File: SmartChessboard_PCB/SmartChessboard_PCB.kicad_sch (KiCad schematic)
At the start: 24 parts, among them J1 USB_C_Receptacle, SW1 SMD_4.6x2.8mm_h2.5mm, SW2 SMD_4.6x2.8mm_h2.5mm, U2 DT1042-04SO, U3 ESP32-S3-MINI, U6 RT9080-3.3

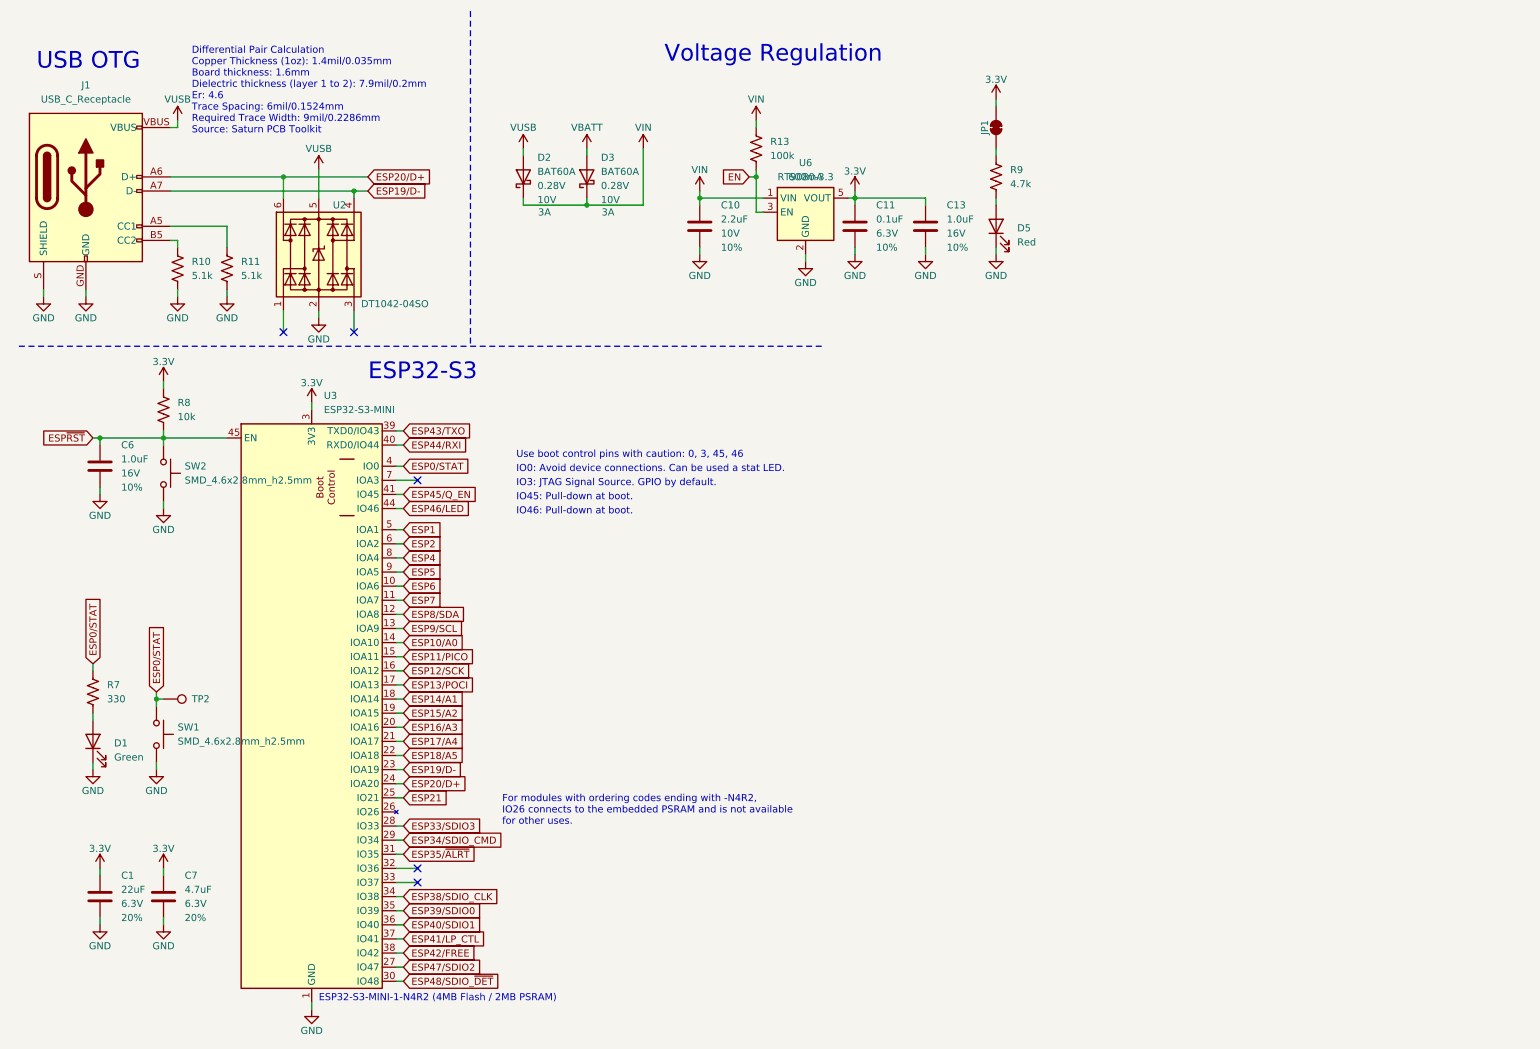
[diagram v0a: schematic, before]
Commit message: LEDs added
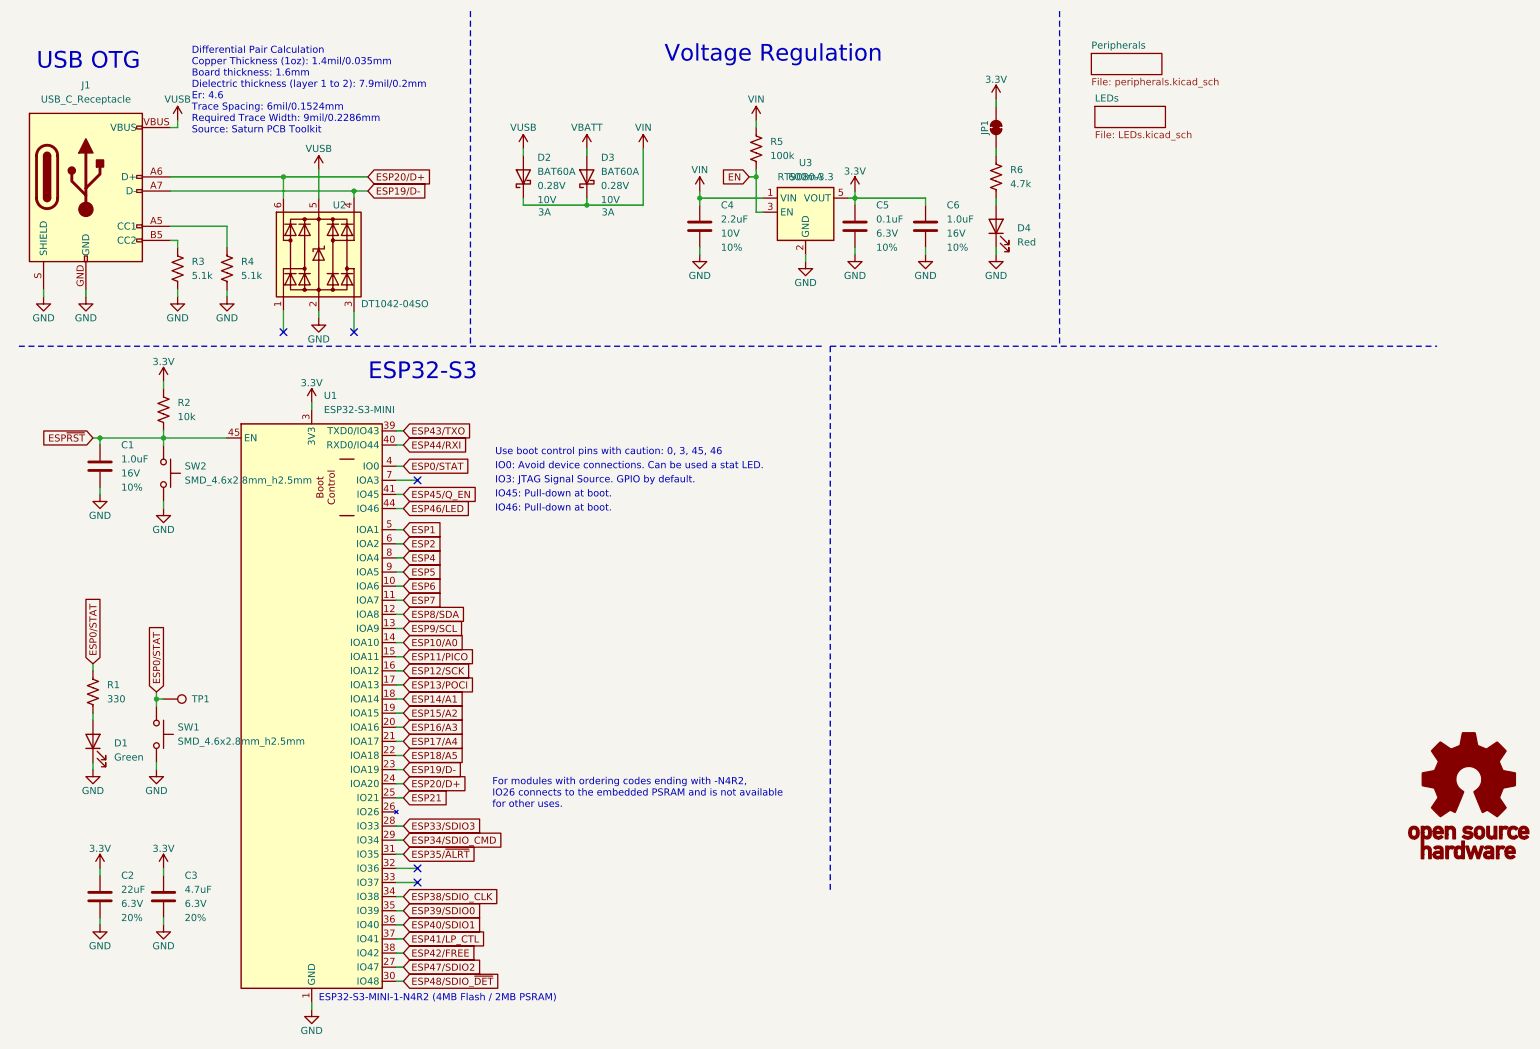
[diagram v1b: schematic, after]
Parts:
- added G1: OSHW_Logo, SparkFun-Aesthetic:Creative_Commons_License, symbol SparkFun-Aesthetic:OSHW_Logo
- renumbered C6 to C1, C1 to C2, C7 to C3, C10 to C4, C11 to C5, C13 to C6, D5 to D4, R7 to R1, R8 to R2, R10 to R3, R11 to R4, R13 to R5, R9 to R6, TP2 to TP1, U3 to U1, U6 to U3
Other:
- added sheet LEDs (LEDs.kicad_sch)
- added sheet Peripherals (peripherals.kicad_sch)

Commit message: before hall sensors
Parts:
- added J4, J5: Conn_01x15, SparkFun-Connector:1x15, symbol SparkFun-Connector:Conn_01x15
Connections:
- net 3.3V: now also J4.14 (Pin_14)
- net EN: now also J5.11 (Pin_11)
- net ESP1: now also J5.3 (Pin_3)
- net ESP10/A0: now also J4.12 (Pin_12)
- net ESP11/PICO: now also J4.5 (Pin_5)
- net ESP12/SCK: now also J4.6 (Pin_6)
- net ESP13/POCI: now also J4.4 (Pin_4)
- net ESP14/A1: now also J4.11 (Pin_11)
- net ESP15/A2: now also J4.10 (Pin_10)
- net ESP16/A3: now also J4.9 (Pin_9)
- net ESP17/A4: now also J4.8 (Pin_8)
- net ESP18/A5: now also J4.7 (Pin_7)
- net ESP2: now also J5.4 (Pin_4)
- net ESP21: now also J5.9 (Pin_9)
- net ESP4: now also J5.5 (Pin_5)
- net ESP42/FREE: now also J4.1 (Pin_1)
- net ESP43/TXO: now also J4.2 (Pin_2)
- net ESP44/RXI: now also J4.3 (Pin_3)
- net ESP5: now also J5.6 (Pin_6)
- net ESP6: now also J5.7 (Pin_7)
- net ESP7: now also J5.8 (Pin_8)
- net ESP8/SDA: now also J5.2 (Pin_2)
- net ESP9/SCL: now also J5.1 (Pin_1)
- net ESP~{RST}: now also J4.15 (Pin_15)
- net GND: now also J4.13 (Pin_13)
- net VBATT: now also J5.12 (Pin_12)
- net VUSB: now also J5.10 (Pin_10)
- net VIN renamed 5V
- no-connect marks 5 -> 8
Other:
- added sheet Hall sensors (hall.kicad_sch)
- note removed: "For modules with ordering codes ending with -N4R2, IO26 connects to the embedded PSRAM and is not available for other uses."
- moved on the sheet: D2, D3

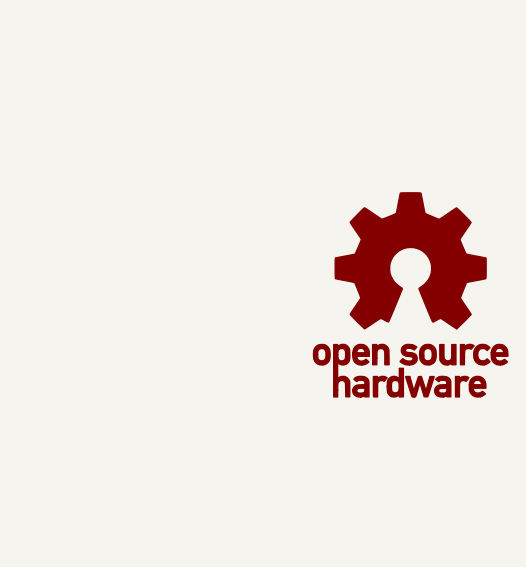
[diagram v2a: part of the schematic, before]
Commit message: level shifter added
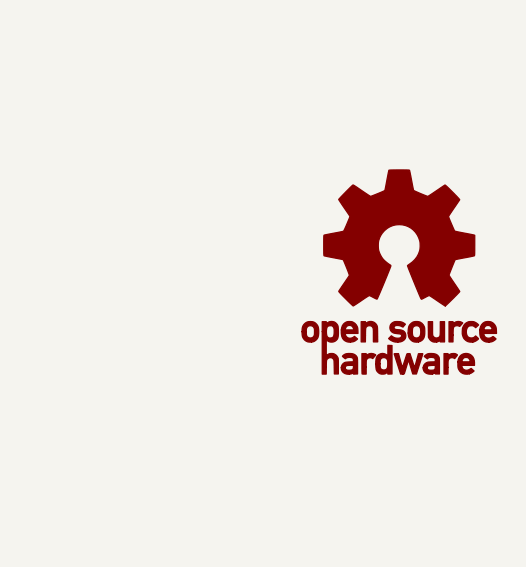
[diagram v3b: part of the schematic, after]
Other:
- title: (none) -> SmartChessboard
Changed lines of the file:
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@@
 	(generator_version "9.0")
 	(paper "A4")
+	(title_block
+		(title "SmartChessboard")
+		(date "2025-08-15")
+		(rev "0")
+		(comment 3 "Released under CERN Open Hardware Licence Version 2")
+		(comment 4 "Designed by: Alessandro Sabbadini")
+	)
 	(text "IO0: Avoid device connections. Can be used a stat LED."
 		(exclude_from_sim no)
@@
 	(symbol
 		(lib_id "SparkFun-Aesthetic:OSHW_Logo")
-		(at 273.05 157.48 0)
+		(at 271.78 154.94 0)
 		(unit 1)
 		(exclude_from_sim no)
@@
 		(fields_autoplaced yes)
 		(property "Reference" "G1"
-			(at 273.05 140.97 0)
+			(at 271.78 138.43 0)
 			(effects
 				(font
@@
 		)
 		(property "Value" "OSHW_Logo"
-			(at 273.05 166.37 0)
+			(at 271.78 163.83 0)
 			(effects
 				(font
@@
 		)
 		(property "Footprint" "SparkFun-Aesthetic:Creative_Commons_License"
-			(at 273.2547 157.5043 0)
+			(at 271.9847 154.9643 0)
 			(effects
 				(font
@@
 		)
 		(property "Datasheet" ""
-			(at 273.2547 157.5043 0)
+			(at 271.9847 154.9643 0)
 			(effects
 				(font
@@
 		)
 		(property "Description" ""
-			(at 273.05 157.48 0)
-			(effects
-				(font
+			(at 271.78 154.94 0)
+			(effects
+				(font

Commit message: psc
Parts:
- removed D2, D3: BAT60A, SparkFun-Semiconductor-Standard:SOD-323, symbol SparkFun-DiscreteSemi:D_Schottky_3A_10V_0.28V
- added D2, D3: BAT60A, Diode_SMD:D_SOD-323, symbol Diode:BAT60A
- renumbered J4 to J2, J5 to J3
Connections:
- net 5V: now also D2.1 (K), D3.1 (K)
- net VUSB: now also D2.2 (A)
- net ESP33/SDIO3 renamed S0
- net ESP34/SDIO_CMD renamed S1
- net ESP38/SDIO_CLK renamed LV_SIG_3
- net ESP39/SDIO0 renamed LV_SIG_4
- net ESP40/SDIO1 renamed LV_SIG_2
- net ESP42/FREE: no longer names the net of J2.1 (Pin_1)
- net ESP42/FREE: no longer U1.38 (IO42)
- net ESP47/SDIO2 renamed S2
- net ESP48/SDIO_~{DET} renamed LV_SIG_1
- net VBATT renamed VDOBOT
- net VDOBOT: now also D3.2 (A)
- new net S3: U1.38 (IO42)
- no-connect marks 8 -> 9

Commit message: pcb finished
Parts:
- added H1, H2, H3, H4: ~, PCM_JLCPCB:Hole, 3mm, symbol PCM_JLCPCB-Manufacturing:Mounting Hole, 3mm, Via Stiched
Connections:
- net EN: now also J2.1 (Pin_1); no longer J3.11 (Pin_11)
- net GND: now also H1.1, H2.1, H3.1, H4.1
